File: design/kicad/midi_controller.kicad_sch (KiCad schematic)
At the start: 5 parts, among them J7 Conn_01x05, U1 CD74HC4067M

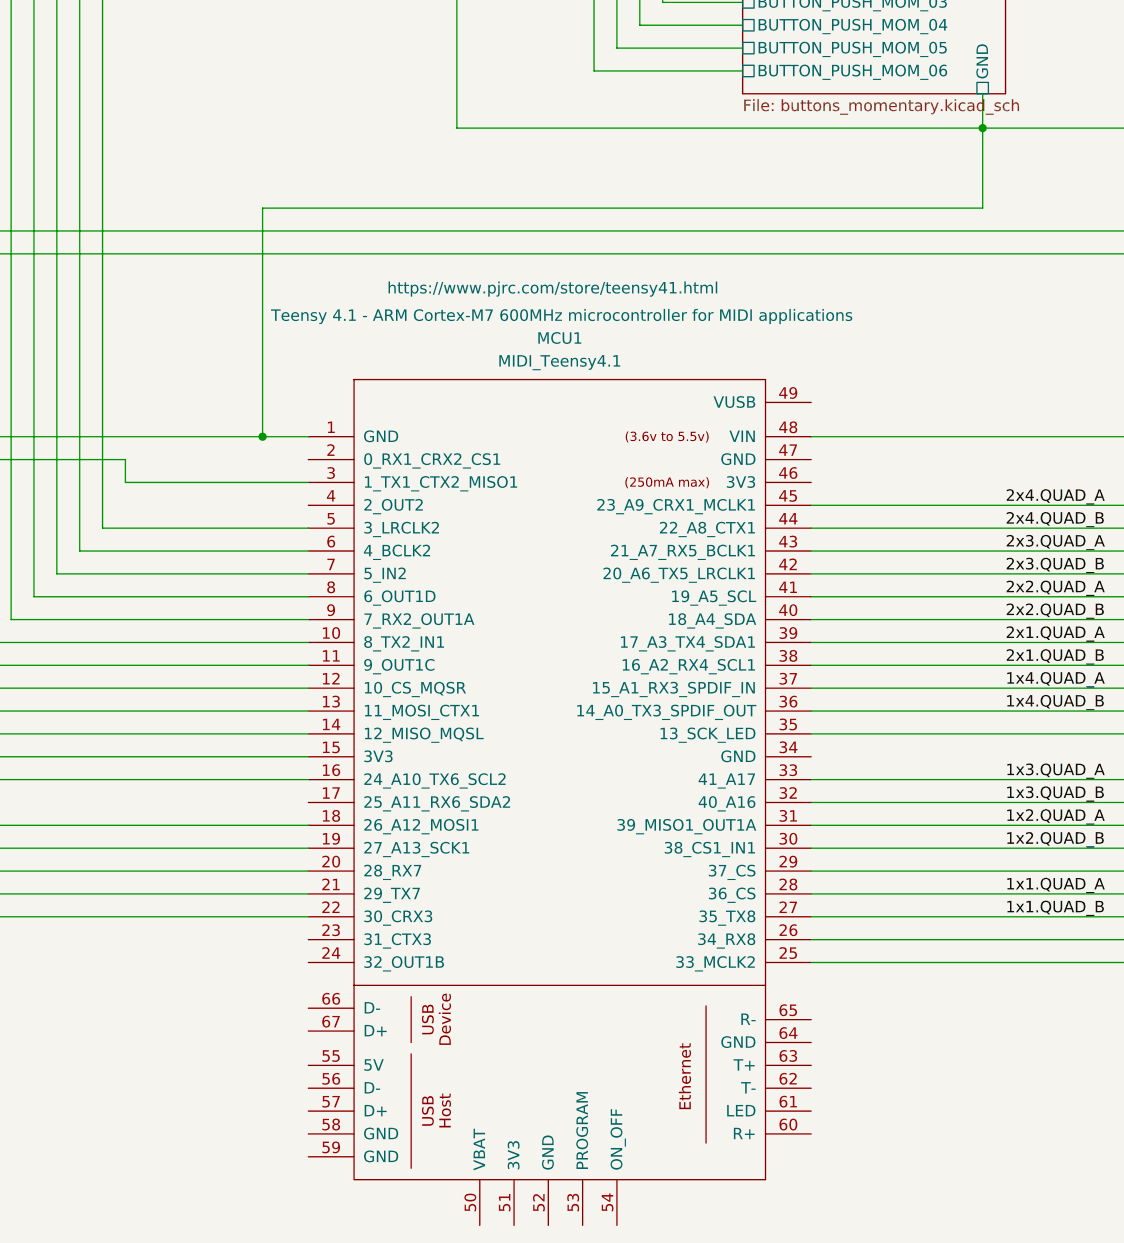
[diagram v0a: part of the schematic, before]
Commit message: Update kicad binary files
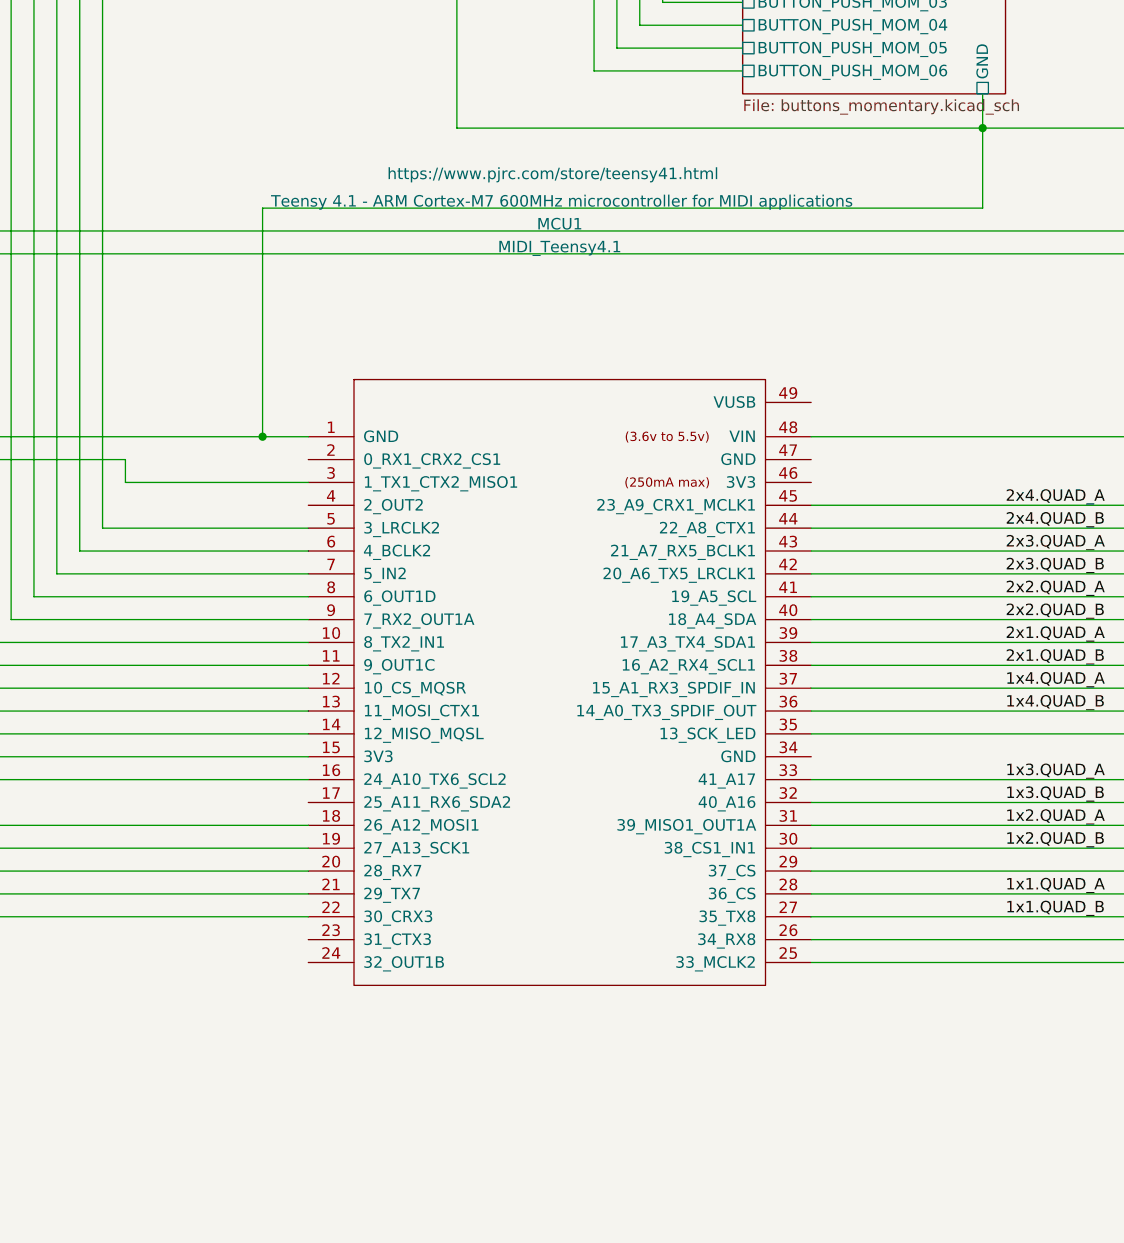
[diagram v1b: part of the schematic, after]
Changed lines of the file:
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@@
 	(symbol
 		(lib_id "midi_controller:MIDI_Teensy4.1")
-		(at 186.69 215.9 0)
+		(at 186.69 203.2 0)
 		(unit 1)
 		(exclude_from_sim no)
@@
 		(dnp no)
 		(property "Reference" "MCU1"
-			(at 186.69 166.878 0)
+			(at 186.69 154.178 0)
 			(effects
 				(font
@@
 		)
 		(property "Value" "MIDI_Teensy4.1"
-			(at 186.69 169.418 0)
+			(at 186.69 156.718 0)
 			(effects
 				(font
@@
 		)
 		(property "Footprint" "midi_controller:Teensy41"
-			(at 186.436 236.728 0)
+			(at 186.436 224.028 0)
 			(effects
 				(font
@@
 		)
 		(property "Datasheet" "https://www.pjrc.com/store/teensy41.html"
-			(at 185.928 161.29 0)
+			(at 185.928 148.59 0)
 			(effects
 				(font
@@
 		)
 		(property "Description" "Teensy 4.1 - ARM Cortex-M7 600MHz microcontroller for MIDI applications"
-			(at 186.944 164.338 0)
+			(at 186.944 151.638 0)
 			(effects
 				(font
@@
 		(pin "42"
 		)
-		(pin "55"
-		)
 		(pin "19"
-		)
-		(pin "53"
-		)
-		(pin "52"
 		)
 		(pin "2"
@@
 		(pin "33"
 		)
-		(pin "58"
-		)
 		(pin "47"
 		)
@@
 		)
 		(pin "45"
-		)
-		(pin "63"
 		)
 		(pin "39"
@@
 		)
 		(pin "13"
-		)
-		(pin "51"
 		)
 		(pin "37"
@@
 		(pin "20"
 		)
-		(pin "59"
-		)
 		(pin "30"
 		)
 		(pin "24"
-		)
-		(pin "57"
-		)
-		(pin "66"
 		)
 		(pin "12"
@@
 		(pin "18"
 		)
-		(pin "54"
-		)
-		(pin "67"
-		)
 		(pin "43"
 		)
-		(pin "50"
-		)
-		(pin "64"
-		)
 		(pin "9"
-		)
-		(pin "56"
 		)
 		(pin "17"
 		)
 		(pin "14"
-		)
-		(pin "61"
-		)
-		(pin "60"
-		)
-		(pin "62"
 		)
 		(pin "36"
@@
 		(pin "11"
 		)
-		(pin "65"
-		)
 		(pin "25"
 		)
@@
 		)
 		(instances
-			(project ""
+			(project "midi_controller"
 				(path "/9e44e663-00d0-4f33-bf1f-c4ad78deb554"
 					(reference "MCU1")

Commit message: Fix hardware pin configuration and rotary encoder parameters
- Updated CS_PIN from 30 to 28 in SystemConstants.hpp to reflect the correct hardware setup for ILI9341.
- Modified rotary encoder parameters in ConfigurationFactory.cpp, changing the first parameter of asRotaryEncoder from 28 to 23 for proper functionality.
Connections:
- net 1x2.QUAD_B is gone; now on net 2x3.QUAD_A: MCU1.30 (38_CS1_IN1)
- net 1x3.QUAD_B is gone; now on net 2x2.QUAD_A: MCU1.32 (40_A16)
- net 1x4.QUAD_B is gone; now on net 2x1.QUAD_A: MCU1.36 (14_A0_TX3_SPDIF_OUT)
- net 2x1.QUAD_B is gone; now on net 1x4.QUAD_A: MCU1.38 (16_A2_RX4_SCL1)
- net 2x2.QUAD_B is gone; now on net 1x3.QUAD_A: MCU1.40 (18_A4_SDA)
- net 2x3.QUAD_B is gone; now on net 1x2.QUAD_A: MCU1.42 (20_A6_TX5_LRCLK1)
- net 2x4.QUAD_B is gone; now on net 1x1.QUAD_A: MCU1.44 (22_A8_CTX1)
- net Buttons_Momentary/GND is gone; now on net GND: D1.2 (GND), J7.4 (Pin_4), J7.5 (Pin_5), MCU1.1 (GND), U1.12 (GND), U1.15 (~{E})
- net 1x1.QUAD_A: now also MCU1.45 (23_A9_CRX1_MCLK1); no longer MCU1.28 (36_CS)
- net 1x2.QUAD_A: now also MCU1.43 (21_A7_RX5_BCLK1); no longer MCU1.31 (39_MISO1_OUT1A)
- net 1x3.QUAD_A: now also MCU1.41 (19_A5_SCL); no longer MCU1.33 (41_A17)
- net 1x4.QUAD_A: now also MCU1.39 (17_A3_TX4_SDA1); no longer MCU1.37 (15_A1_RX3_SPDIF_IN)
- net 2x1.QUAD_A: now also MCU1.37 (15_A1_RX3_SPDIF_IN); no longer MCU1.39 (17_A3_TX4_SDA1)
- net 2x2.QUAD_A: now also MCU1.33 (41_A17); no longer MCU1.41 (19_A5_SCL)
- net 2x3.QUAD_A: now also MCU1.31 (39_MISO1_OUT1A); no longer MCU1.43 (21_A7_RX5_BCLK1)
- net 2x4.QUAD_A: now also MCU1.28 (36_CS), MCU1.29 (37_CS); no longer MCU1.45 (23_A9_CRX1_MCLK1)
- net Encoder with Push Button_Navigation/QUAD_A: no longer MCU1.21 (29_TX7)
- net Encoder with Push Button_Navigation/QUAD_B: no longer MCU1.22 (30_CRX3)
- net +3V3: now reaches MCU1.15 (3V3), U1.24 (VCC)
- net +3V3: now also D1.8 (LED), MCU1.46 (3V3); no longer D1.1 (VCC)
- net at D1.10 (T_CLK): no longer MCU1.19 (27_A13_SCK1)
- net at D1.11 (T_CS): no longer MCU1.20 (28_RX7)
- net at D1.12 (T_DIN): no longer MCU1.18 (26_A12_MOSI1)
- net at D1.13 (T_DO): no longer MCU1.3 (1_TX1_CTX2_MISO1)
- net at D1.14 (T_IRQ): no longer MCU1.16 (24_A10_TX6_SCL2)
- net at D1.3 (CS): now also MCU1.20 (28_RX7); no longer MCU1.12 (10_CS_MQSR)
- net at D1.4 (RST): now also MCU1.21 (29_TX7); no longer MCU1.11 (9_OUT1C)
- net at D1.5 (DC): now also MCU1.2 (0_RX1_CRX2_CS1); no longer MCU1.29 (37_CS)
- net at D1.6 (SDI/MOSI): now also MCU1.18 (26_A12_MOSI1); no longer MCU1.13 (11_MOSI_CTX1)
- net at D1.7 (SCK): now also MCU1.19 (27_A13_SCK1); no longer MCU1.35 (13_SCK_LED)
- net at MCU1.10 (8_TX2_IN1): no longer D1.8 (LED)
- net at D1.9 (SDO/MISO): now also MCU1.3 (1_TX1_CTX2_MISO1); no longer MCU1.14 (12_MISO_MQSL)
- net at MCU1.9 (7_RX2_OUT1A): no longer U1.1 (COM)
- net S0: now reaches U1.10 (S0)
- net S0: now also MCU1.5 (3_LRCLK2); no longer MCU1.8 (6_OUT1D)
- net S1: now reaches U1.11 (S1)
- net S1: now also MCU1.6 (4_BCLK2); no longer MCU1.7 (5_IN2)
- net S3: now reaches U1.13 (S3)
- net S3: now also MCU1.8 (6_OUT1D); no longer MCU1.5 (3_LRCLK2)
- net S2: now reaches U1.14 (S2)
- net S2: now also MCU1.7 (5_IN2); no longer MCU1.6 (4_BCLK2)
- net ENC_B_NAV: now reaches J7.3 (Pin_3), MCU1.25 (33_MCLK2)
- net ENC_A_NAV: now reaches J7.2 (Pin_2), MCU1.26 (34_RX8)
- net GND: now reaches MCU1.34 (GND)
- net GND: now also MCU1.47 (GND)
- net COM: now reaches MCU1.4 (2_OUT2)
- net COM: now also U1.1 (COM)
- net +5V: now reaches J7.1 (Pin_1), MCU1.48 (VIN)
- net +5V: now also D1.1 (VCC)
- net 1x1.QUAD_B: no longer names the net of MCU1.27 (35_TX8)
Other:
- moved on the sheet: D1, ENC_OPT1, J7, U1

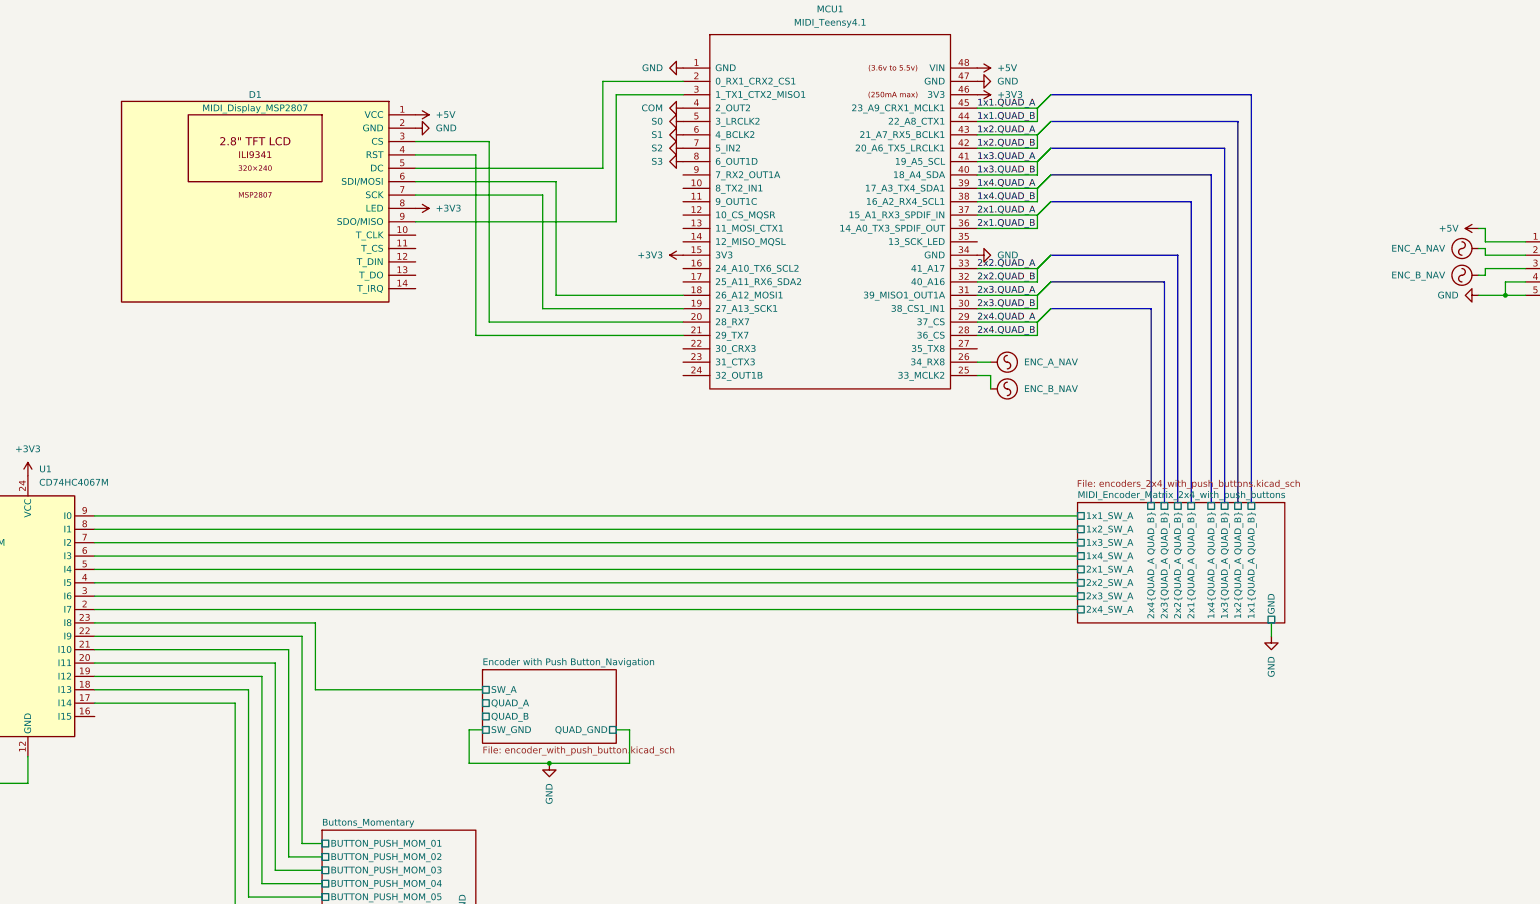
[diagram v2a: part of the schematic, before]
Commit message: Update kicad binary files
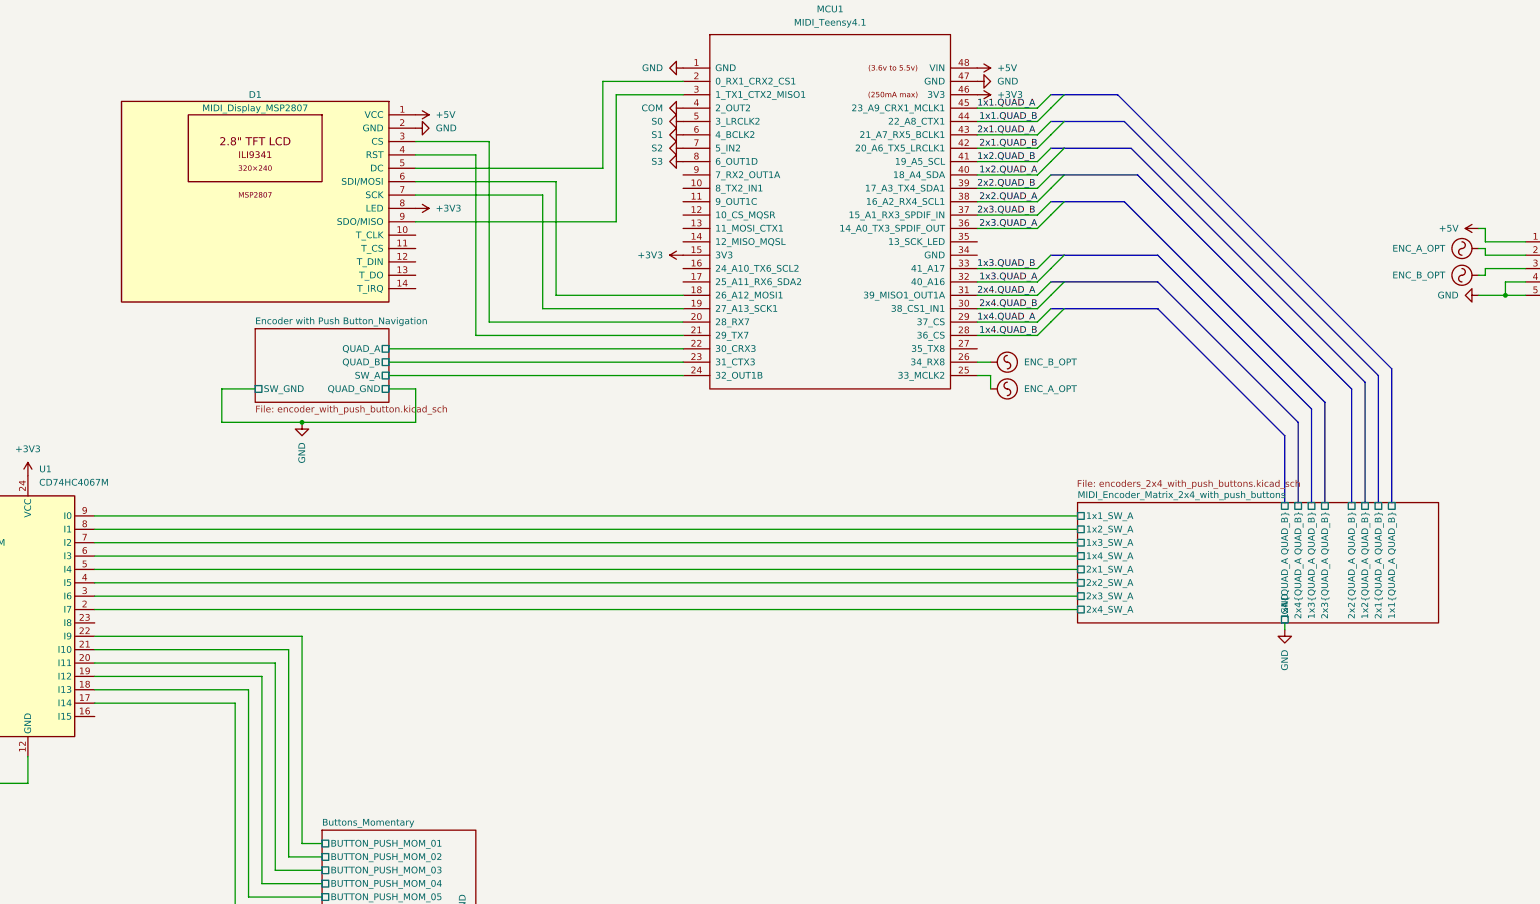
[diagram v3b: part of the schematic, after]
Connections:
- net 1x1.QUAD_A: no longer MCU1.44 (22_A8_CTX1)
- net 1x2.QUAD_A: now also MCU1.40 (18_A4_SDA); no longer MCU1.42 (20_A6_TX5_LRCLK1), MCU1.43 (21_A7_RX5_BCLK1)
- net 1x3.QUAD_A: now also MCU1.32 (40_A16); no longer MCU1.40 (18_A4_SDA), MCU1.41 (19_A5_SCL)
- net 1x4.QUAD_A: now also MCU1.29 (37_CS); no longer MCU1.38 (16_A2_RX4_SCL1), MCU1.39 (17_A3_TX4_SDA1)
- net 2x1.QUAD_A: now also MCU1.43 (21_A7_RX5_BCLK1); no longer MCU1.36 (14_A0_TX3_SPDIF_OUT), MCU1.37 (15_A1_RX3_SPDIF_IN)
- net 2x2.QUAD_A: now also MCU1.38 (16_A2_RX4_SCL1); no longer MCU1.32 (40_A16), MCU1.33 (41_A17)
- net 2x3.QUAD_A: now also MCU1.36 (14_A0_TX3_SPDIF_OUT); no longer MCU1.30 (38_CS1_IN1), MCU1.31 (39_MISO1_OUT1A)
- net 2x4.QUAD_A: now also MCU1.31 (39_MISO1_OUT1A); no longer MCU1.28 (36_CS), MCU1.29 (37_CS)
- net Encoder with Push Button_Navigation/QUAD_A: now also MCU1.22 (30_CRX3)
- net Encoder with Push Button_Navigation/QUAD_B: now also MCU1.23 (31_CTX3)
- net Encoder with Push Button_Navigation/SW_A: now also MCU1.24 (32_OUT1B); no longer U1.23 (I8)
- net GND: no longer MCU1.34 (GND)
- net ENC_A_NAV renamed ENC_A_OPT
- net ENC_A_OPT: now also MCU1.25 (33_MCLK2); no longer MCU1.26 (34_RX8)
- net ENC_B_NAV renamed ENC_B_OPT
- net ENC_B_OPT: now also MCU1.26 (34_RX8); no longer MCU1.25 (33_MCLK2)
- new net 1x1.QUAD_B: MCU1.44 (22_A8_CTX1)
- new net 1x2.QUAD_B: MCU1.41 (19_A5_SCL)
- new net 1x3.QUAD_B: MCU1.33 (41_A17)
- new net 1x4.QUAD_B: MCU1.28 (36_CS)
- new net 2x1.QUAD_B: MCU1.42 (20_A6_TX5_LRCLK1)
- new net 2x2.QUAD_B: MCU1.39 (17_A3_TX4_SDA1)
- new net 2x3.QUAD_B: MCU1.37 (15_A1_RX3_SPDIF_IN)
- new net 2x4.QUAD_B: MCU1.30 (38_CS1_IN1)

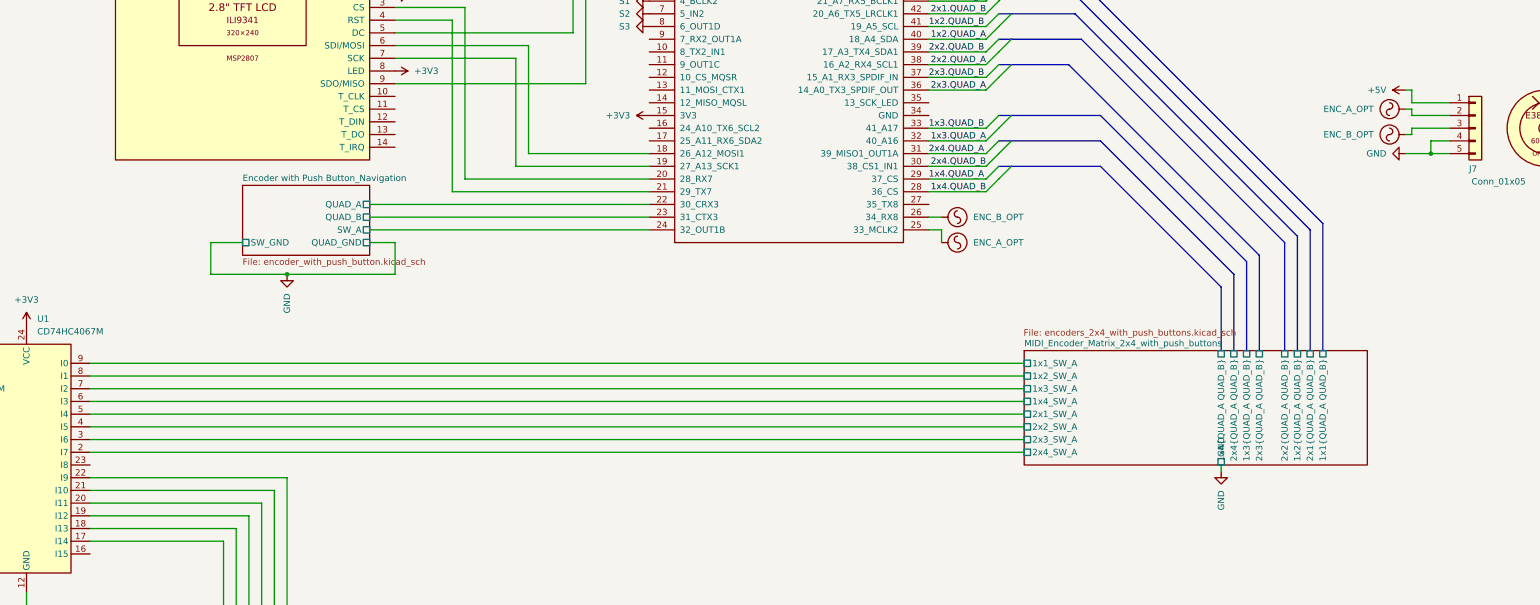
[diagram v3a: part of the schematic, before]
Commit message: Refactor MIDI controller design files: updated active layer, adjusted hidden nets, and modified junction coordinates in schematic. Enhanced layout for better clarity and organization.
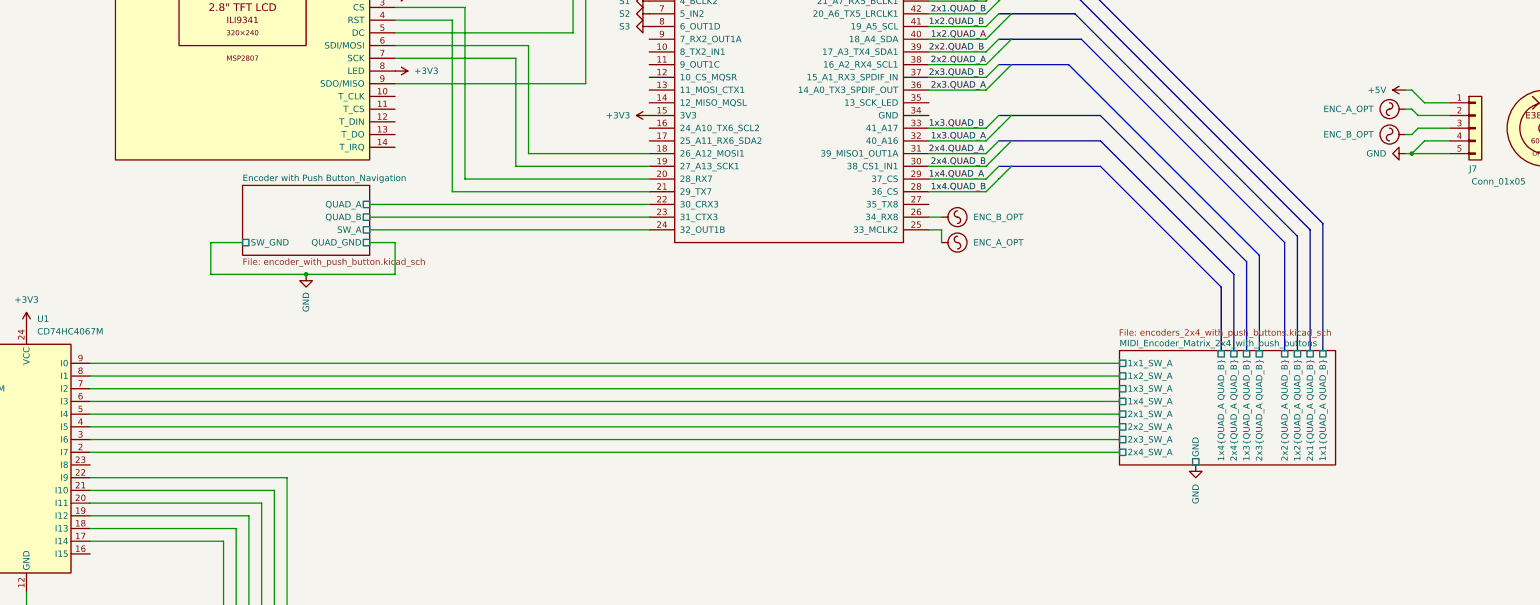
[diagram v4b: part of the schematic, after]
